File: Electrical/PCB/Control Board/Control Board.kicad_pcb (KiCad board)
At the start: 2 copper layers, 154 x 175 mm, 88 parts, among them J1 ED2627-ND, J10 6posheader, J11 S7038-ND, J13 ED1501-ND, J14 ED2989-ND-USB, J15 ED2580-ND, J16 ED2580-ND, J17 ED2744-ND, J18 ED2744-ND, J19 ED2744-ND, J2 ED2627-ND, J20 ED2744-ND, J21 ED2744-ND, J22 ED2744-ND, J23 ED2744-ND, J24 ED2744-ND, J25 ED2744-ND, J26 ED2744-ND, J28 ED2580-ND, J3 ED2627-ND, J4 ED2627-ND, J5 ED2627-ND, J6 S9175-ND, J7 S9175-ND, J8 6posheader, J9 S7038-ND, M1 Mounting_Holes, T1 test_point, T10 test_point, T11 test_point, T12 test_point, T13 test_point, T14 test_point, T15 test_point, T16 test_point, T17 test_point, T18 test_point, T19 test_point, T2 test_point, T20 test_point, T21 test_point, T3 test_point, T4 test_point, T5 test_point, T6 test_point, T7 test_point, T8 test_point, T9 test_point, U1 LM358-N, U2 LM358-N, y1 rover_silkscreen

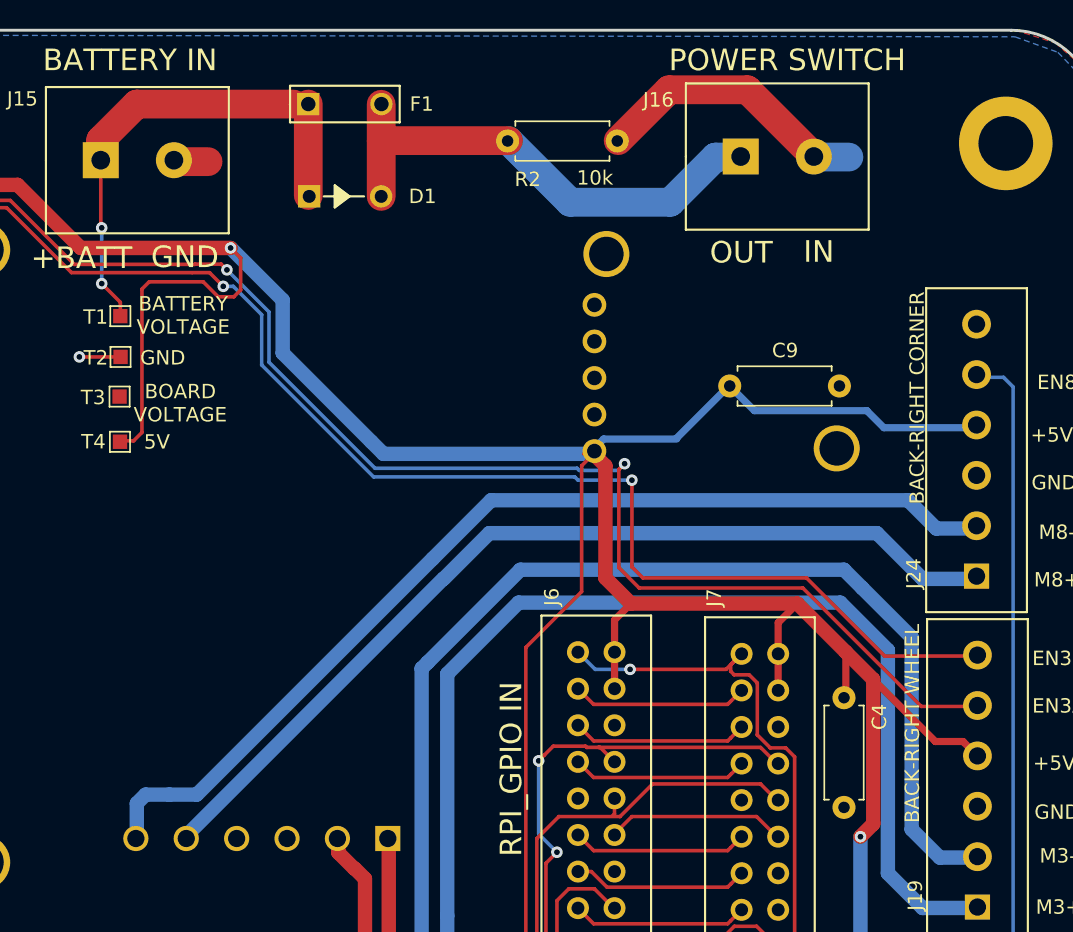
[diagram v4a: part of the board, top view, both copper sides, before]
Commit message: Updated battery, switch, and meter connections
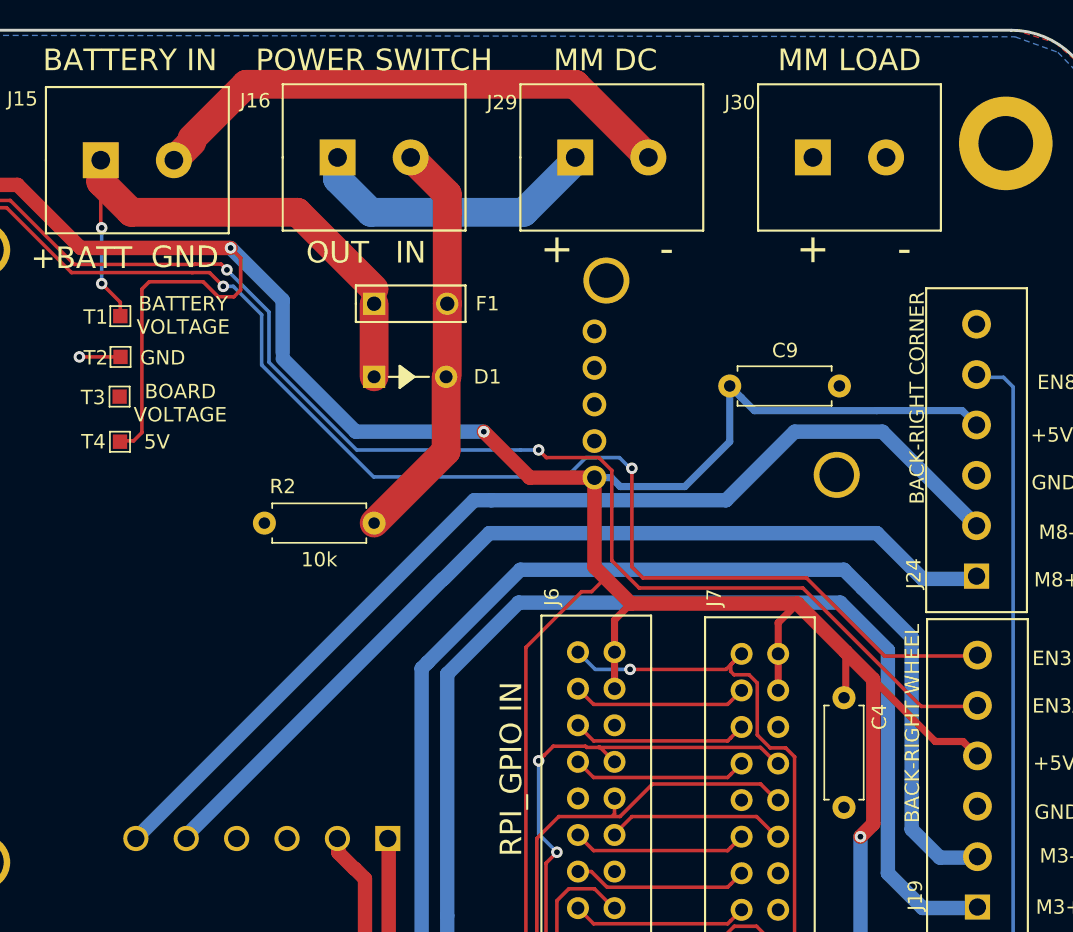
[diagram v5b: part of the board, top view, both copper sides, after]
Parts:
- added J29: ED2580-ND, JPL Robotics:ED2580-ND, F.Cu at (116.7, -165.2)
- added J30: ED2580-ND, JPL Robotics:ED2580-ND, F.Cu at (133.2, -165.2)
- moved R2 28.1 mm to (102.7, -139.8), turned to 180 degrees
- moved J16 28.0 mm to (100.2, -165.2)
- moved F1 14.6 mm to (102.7, -155.0)
- moved D1 13.3 mm to (102.7, -149.9)
- moved J9 1.84 mm to (116.8, -158.8)
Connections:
- net Net-(D1-Pad1) renamed /BATTPOS
- D1 pad 2: Net-(D1-Pad2) -> /SWIN
- F1 pad 2: Net-(D1-Pad2) -> /SWIN
- J15 pad 2: GND -> /BATTNEG
- J16 pad 1: Net-(D1-Pad2) -> /MMDC+
- J16 pad 2: +BATT -> /SWIN
- R2 pad 1: Net-(D1-Pad2) -> /SWIN
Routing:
- net /BATTNEG: track 0.00 -> 37.4 mm
- net Net-(D1-Pad2): track 34.5 -> 0.00 mm
- net /SWIN: track 0.00 -> 28.6 mm
- net /MMDC+: track 0.00 -> 20.4 mm
- net +BATT: track 20.9 -> 1.50 mm
- net +5V: track 1306.8 -> 1300.2 mm, vias 22 -> 23
- net /BATTPOS: track 34.7 -> 41.0 mm
- net /RC4M2B: track 70.2 -> 72.8 mm
- net GND: track 29.3 -> 26.9 mm
- net /RC2EN1A: track 108.8 -> 107.3 mm
- net /RC2EN1B: track 107.4 -> 108.9 mm
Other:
- board text added: "MM DC"
- board text added: "MM LOAD"

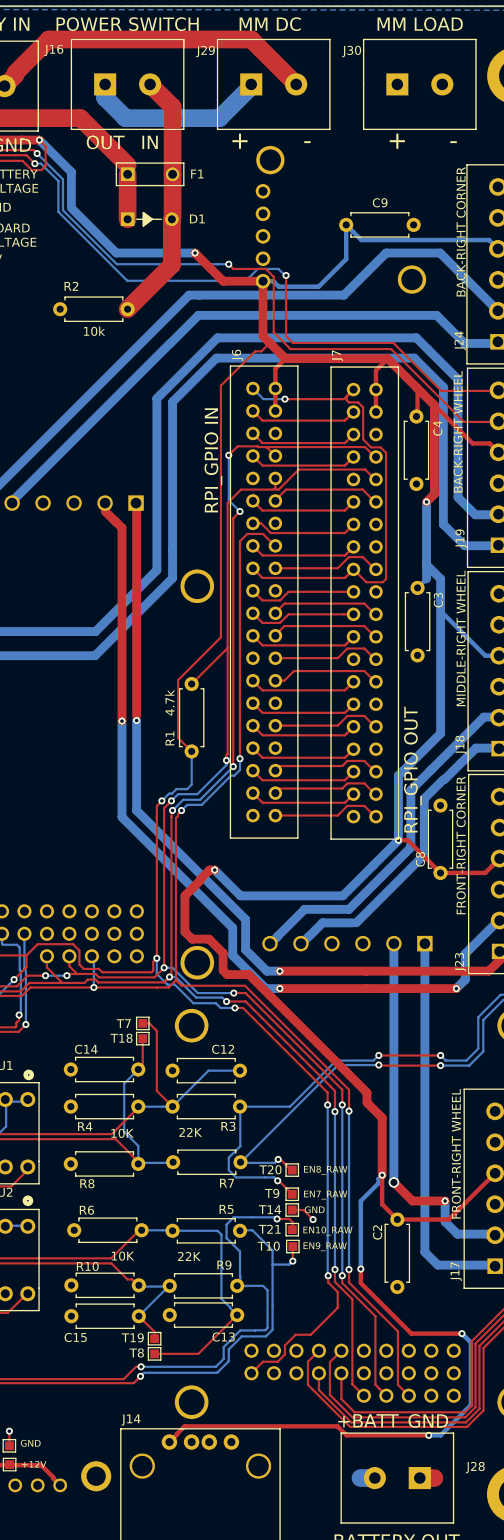
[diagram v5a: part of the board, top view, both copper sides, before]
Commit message: Moved R2 to prepare for possibly adding voltage and current monitoring
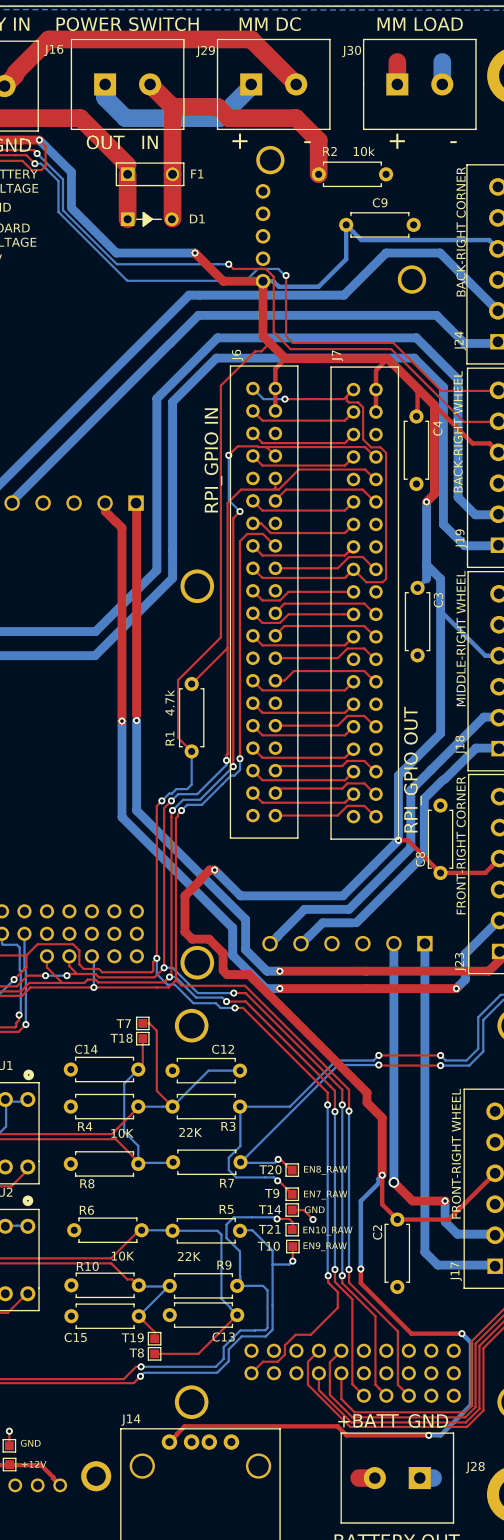
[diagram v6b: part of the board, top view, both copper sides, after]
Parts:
- moved R2 26.4 mm to (124.3, -155.0), turned to 0 degrees
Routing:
- net /SWIN: track 28.6 -> 38.2 mm
- net +BATT: track 1.50 -> 4.31 mm
- net GND: track 26.9 -> 29.2 mm
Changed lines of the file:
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@@
     (thickness 1.6)
     (drawings 169)
-    (tracks 1724)
+    (tracks 1729)
     (zones 0)
     (modules 90)
@@
   )
   (module Resistor_THT:R_Axial_DIN0207_L6.3mm_D2.5mm_P7.62mm_Horizontal (layer F.Cu)
-    (at 102.743 -139.7635 180)
+    (at 124.333 -155.0035)
     (descr "Resistor, Axial_DIN0207 series, Axial, Horizontal, pin pitch=7.62mm, 0.25W = 1/4W, length*diameter=6.3*2.5mm^2, http://cdn-reichelt.de/documents/datenblatt/B400/1_4W%23YAG.pdf")
     (tags "Resistor Axial_DIN0207 series Axial Horizontal pin pitch 7.62mm 0.25W = 1/4W length 6.3mm diameter 2.5mm")
-    (fp_text reference R2 (at 6.35 2.54) (layer F.SilkS)
+    (fp_text reference R2 (at 1.27 -2.54) (layer F.SilkS)
       (effects (font (size 1 1) (thickness 0.15)))
     )
@@
     (fp_line (start 0.66 1.25) (end 6.96 1.25) (layer F.Fab) (width 0.1))
     (fp_line (start 0.66 -1.25) (end 0.66 1.25) (layer F.Fab) (width 0.1))
-    (pad 2 thru_hole oval (at 7.62 0 180) (size 1.6 1.6) (drill 0.8) (layers *.Cu *.Mask)
+    (pad 2 thru_hole oval (at 7.62 0) (size 1.6 1.6) (drill 0.8) (layers *.Cu *.Mask)
       (net 26 +BATT))
-    (pad 1 thru_hole circle (at 0 0 180) (size 1.6 1.6) (drill 0.8) (layers *.Cu *.Mask)
+    (pad 1 thru_hole circle (at 0 0) (size 1.6 1.6) (drill 0.8) (layers *.Cu *.Mask)
       (net 179 /SWIN))
     (model ${KISYS3DMOD}/Resistor_THT.3dshapes/R_Axial_DIN0207_L6.3mm_D2.5mm_P7.62mm_Horizontal.wrl
@@
     (effects (font (size 1.5 1.5) (thickness 0.3)))
   )
-  (gr_text 10k (at 98.933 -137.2235) (layer F.SilkS)
+  (gr_text 10k (at 129.413 -157.5435) (layer F.SilkS)
     (effects (font (size 1 1) (thickness 0.1)))
   )
@@
   (segment (start 119.8245 -41.275) (end 121.3485 -39.751) (width 0.25) (layer F.Cu) (net 17))
   (segment (start 119.6975 -41.275) (end 119.8245 -41.275) (width 0.25) (layer F.Cu) (net 17))
-  (segment (start 135.646234 -7.6835) (end 137.414 -7.6835) (width 2) (layer F.Cu) (net 18))
+  (segment (start 128.915234 -7.6835) (end 130.683 -7.6835) (width 2) (layer F.Cu) (net 26))
   (segment (start 73.545 -38.1635) (end 72.5805 -39.128) (width 0.25) (layer F.Cu) (net 18))
   (segment (start 74.295 -38.1635) (end 73.545 -38.1635) (width 0.25) (layer F.Cu) (net 18))
@@
   (segment (start 114.681 -116.1415) (end 114.681 -88.0745) (width 0.25) (layer F.Cu) (net 24))
   (segment (start 115.443 -116.9035) (end 114.681 -116.1415) (width 0.25) (layer F.Cu) (net 24))
-  (segment (start 130.556 -7.6835) (end 129.056 -7.6835) (width 2) (layer B.Cu) (net 26))
+  (segment (start 137.263 -7.6835) (end 135.763 -7.6835) (width 2) (layer B.Cu) (net 18))
+  (segment (start 138.303 -165.1635) (end 138.303 -167.7035) (width 2) (layer B.Cu) (net 18))
+  (segment (start 133.223 -165.1635) (end 133.223 -167.7035) (width 2) (layer F.Cu) (net 26))
   (segment (start 65.913 -41.4655) (end 65.913 -49.5935) (width 0.25) (layer B.Cu) (net 27))
   (segment (start 65.913 -49.5935) (end 66.8655 -50.546) (width 0.25) (layer B.Cu) (net 27))
@@
   (segment (start 107.823 -150.0035) (end 107.743 -149.9235) (width 0.25) (layer F.Cu) (net 179))
   (segment (start 107.823 -155.0035) (end 107.823 -150.0035) (width 2) (layer F.Cu) (net 179))
-  (segment (start 107.743 -144.7635) (end 102.743 -139.7635) (width 2) (layer F.Cu) (net 179))
-  (segment (start 107.743 -149.9235) (end 107.743 -144.7635) (width 2) (layer F.Cu) (net 179))
   (segment (start 107.823 -161.3535) (end 107.823 -155.0035) (width 2) (layer F.Cu) (net 179))
   (segment (start 107.823 -162.6235) (end 107.823 -161.3535) (width 2) (layer F.Cu) (net 179))
   (segment (start 105.283 -165.1635) (end 107.823 -162.6235) (width 2) (layer F.Cu) (net 179))
+  (segment (start 107.823 -162.6235) (end 112.903 -162.6235) (width 2) (layer F.Cu) (net 179))
+  (segment (start 112.903 -162.6235) (end 114.173 -161.3535) (width 2) (layer F.Cu) (net 179))
+  (segment (start 114.173 -161.3535) (end 121.793 -161.3535) (width 2) (layer F.Cu) (net 179))
+  (segment (start 121.793 -161.3535) (end 124.333 -158.8135) (width 2) (layer F.Cu) (net 179))
+  (segment (start 124.333 -158.8135) (end 124.333 -155.0035) (width 2) (layer F.Cu) (net 179))
   (via (at 83.82 -160.274) (size 0.8) (drill 0.4) (layers F.Cu B.Cu) (net 180))
   (segment (start 83.7565 -164.8714) (end 83.7565 -160.3375) (width 0.25) (layer F.Cu) (net 180))

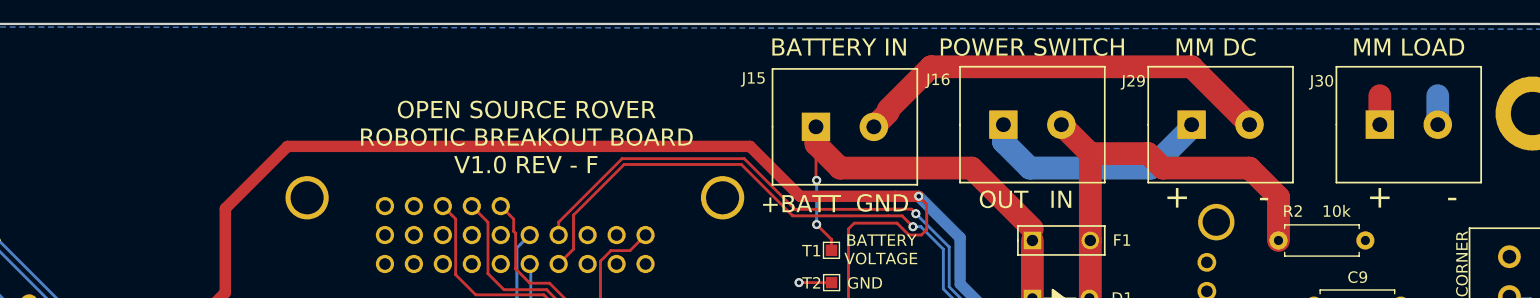
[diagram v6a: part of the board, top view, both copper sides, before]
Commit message: Added digital voltage and current monitoring
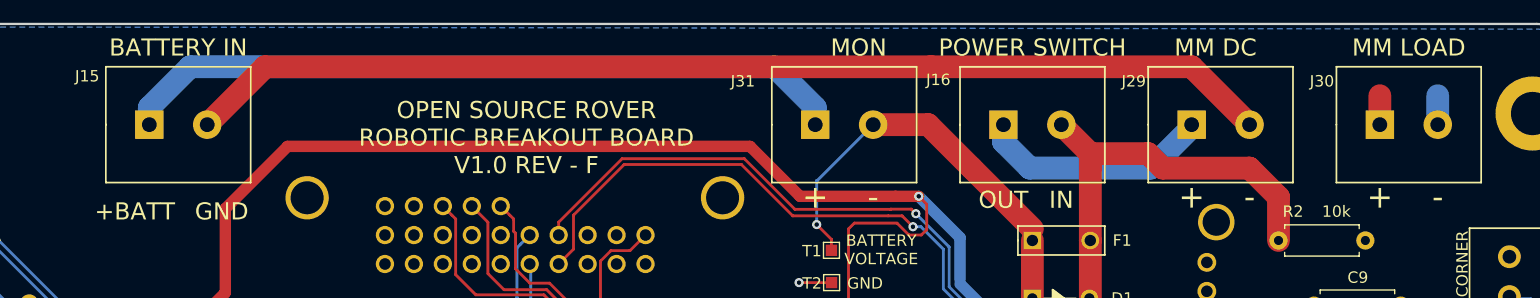
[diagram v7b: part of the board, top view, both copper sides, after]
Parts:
- added J31: ED2580-ND, JPL Robotics:ED2580-ND, F.Cu at (83.7, -165.2)
- moved J15 58.5 mm to (25.3, -165.2)
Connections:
- D1 pad 1: /BATTPOS -> Net-(D1-Pad1)
- F1 pad 1: /BATTPOS -> Net-(D1-Pad1)
- T1 pad 1: /BATTPOS -> Net-(D1-Pad1)
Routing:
- net /BATTNEG: track 37.4 -> 95.6 mm
- net Net-(D1-Pad1): track 0.00 -> 37.5 mm, vias 0 -> 1
- net /BATTPOS: track 41.0 -> 64.4 mm, vias 2 -> 0
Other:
- board text added: "MON"
